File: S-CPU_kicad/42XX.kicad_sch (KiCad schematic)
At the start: 161 parts, among them U34 OR_2, U35 OR_2, U36 OR_2, U37 OR_2, U6 MUX, U6 MUXI

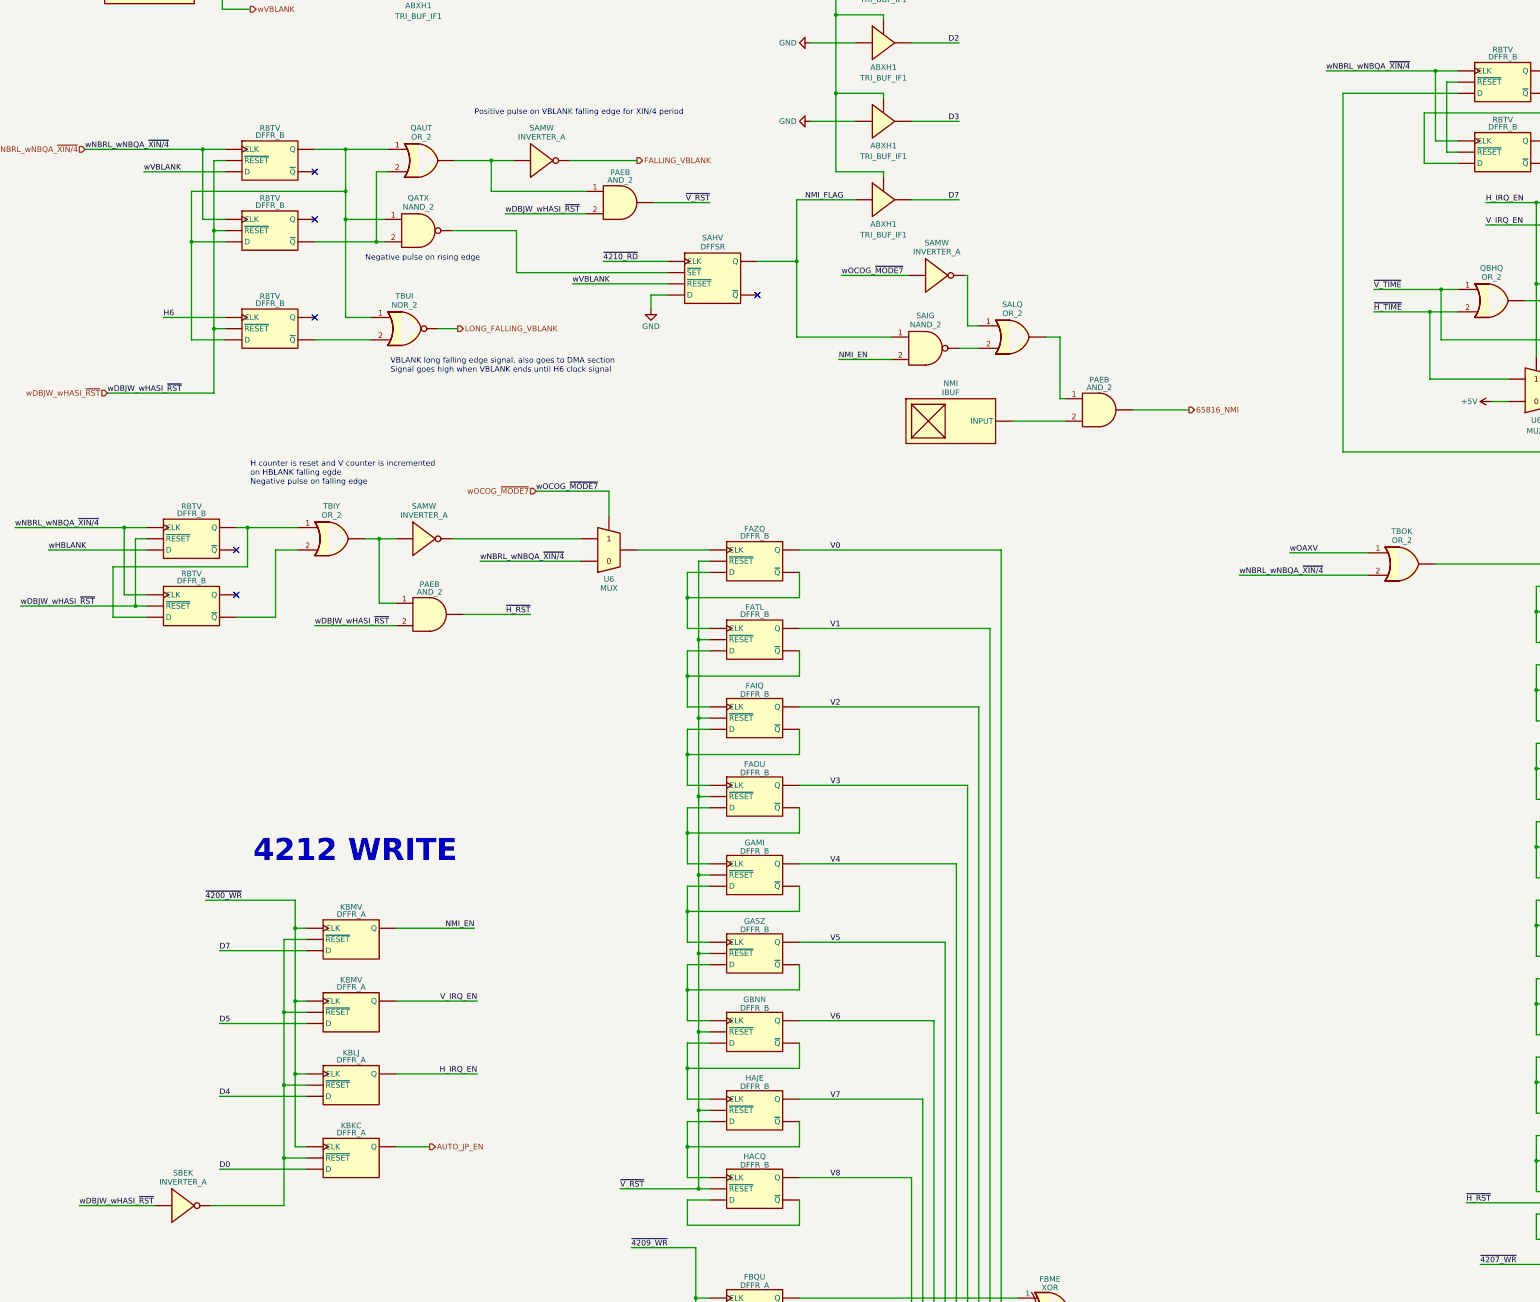
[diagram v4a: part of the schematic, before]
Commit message: Identified some DFFs as being DFFs with SET input rather than RESET input. It helps explaining a lot of beahiour in the MUL/DIV section and in the DMA section.
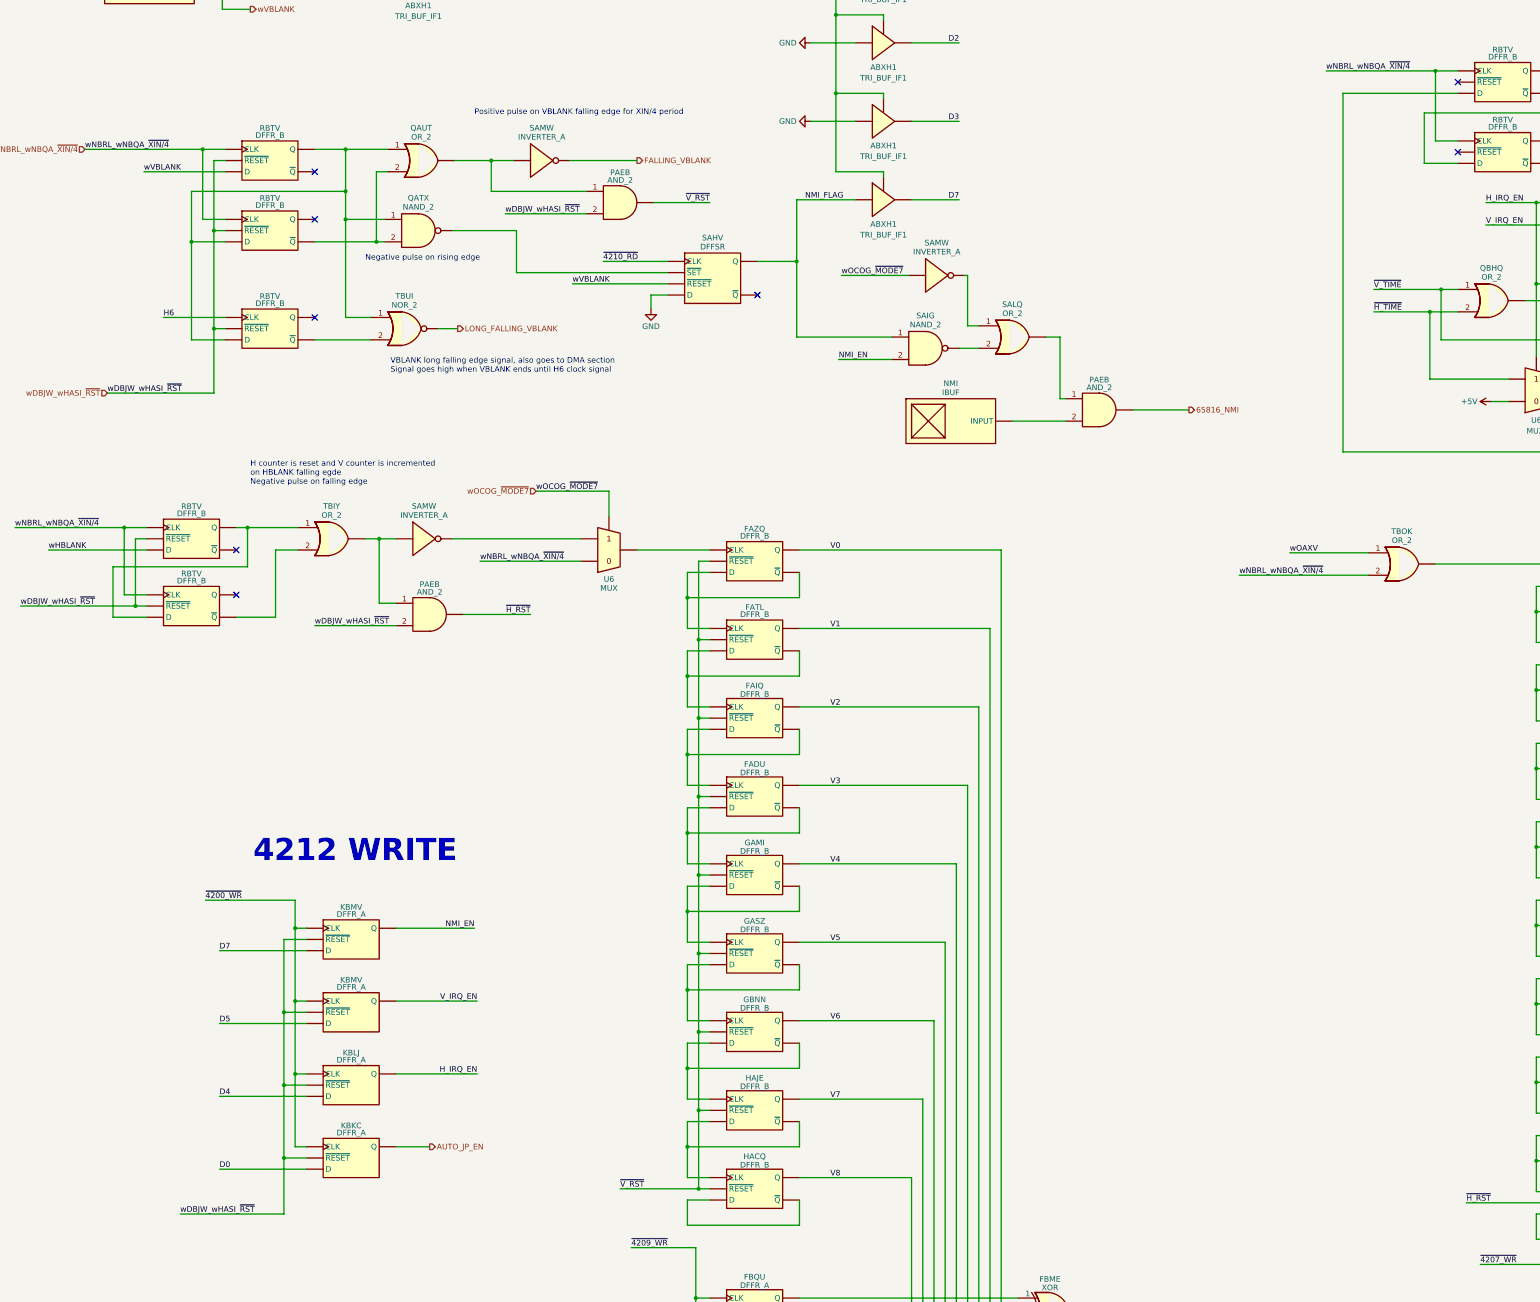
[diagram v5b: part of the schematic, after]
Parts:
- removed SBEK: INVERTER_A, symbol Ricoh_Cells:INVERTER_A
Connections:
- net wDBJW_wHASI_~{RST}: now also KBKC.1 (~{RESET}), KBKC.5 (~{RESET}), KBLJ.1 (~{RESET}), KBLJ.5 (~{RESET}), KBMV.1 (~{RESET}), KBMV.1 (~{RESET}), KBMV.5 (~{RESET}), KBMV.5 (~{RESET})
- net at RBTV.1 (~{RESET}), RBTV.5 (~{RESET}): no longer RBTV.1 (~{RESET}), RBTV.5 (~{RESET})
- new net: RBTV.1 (~{RESET}), RBTV.5 (~{RESET})
- no-connect marks 26 -> 28
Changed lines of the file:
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@@
   (no_connect (at 415.29 476.25))
   (no_connect (at 607.695 400.05))
+  (no_connect (at 584.835 133.985))
   (no_connect (at 325.755 149.225))
   (no_connect (at 415.29 503.555))
@@
   (no_connect (at 415.29 422.91))
   (no_connect (at 325.755 171.45))
+  (no_connect (at 584.835 118.11))
   (no_connect (at 607.695 507.365))
   (no_connect (at 415.29 396.24))
@@
     (stroke (width 0) (type default))
   )
-  (wire (pts (xy 302.26 372.745) (xy 318.77 372.745))
-    (stroke (width 0) (type default))
-  )
   (wire (pts (xy 406.4 412.115) (xy 415.29 412.115))
     (stroke (width 0) (type default))
@@
     (stroke (width 0) (type default))
   )
-  (wire (pts (xy 584.835 133.985) (xy 582.295 133.985))
-    (stroke (width 0) (type default))
-  )
   (wire (pts (xy 120.015 500.38) (xy 147.32 500.38))
     (stroke (width 0) (type default))
@@
     (stroke (width 0) (type default))
   )
-  (wire (pts (xy 318.77 361.95) (xy 318.77 372.745))
+  (wire (pts (xy 318.77 361.95) (xy 318.77 374.65))
     (stroke (width 0) (type default))
   )
@@
     (stroke (width 0) (type default))
   )
-  (wire (pts (xy 582.295 133.985) (xy 582.295 118.11))
-    (stroke (width 0) (type default))
-  )
   (wire (pts (xy 304.8 77.47) (xy 304.8 83.82))
     (stroke (width 0) (type default))
@@
     (stroke (width 0) (type default))
   )
-  (wire (pts (xy 272.415 372.745) (xy 289.56 372.745))
+  (wire (pts (xy 295.275 374.65) (xy 318.77 374.65))
     (stroke (width 0) (type default))
   )
@@
     (stroke (width 0) (type default))
   )
-  (wire (pts (xy 584.835 118.11) (xy 582.295 118.11))
-    (stroke (width 0) (type default))
-  )
   (wire (pts (xy 481.33 224.155) (xy 435.61 224.155))
     (stroke (width 0) (type default))
@@
     (effects (font (size 1.27 1.27)) (justify right bottom))
   )
-  (label "wDBJW_wHASI_~{RST}" (at 272.415 372.745 0) (fields_autoplaced)
+  (label "wDBJW_wHASI_~{RST}" (at 295.275 374.65 0) (fields_autoplaced)
     (effects (font (size 1.27 1.27)) (justify left bottom))
   )
@@
         )
       )
-    )
-  )
-  (symbol (lib_id "Ricoh_Cells:INVERTER_A") (at 295.91 372.745 0) (unit 1)
-    (in_bom yes) (on_board yes) (dnp no) (fields_autoplaced)
-    (property "Reference" "SBEK" (at 295.91 365.355 0)
-      (effects (font (size 1.27 1.27)))
-    )
-    (property "Value" "INVERTER_A" (at 295.91 367.403 0)
-      (effects (font (size 1.27 1.27)))
-    )
-    (property "Footprint" "" (at 293.37 372.745 0)
-      (effects (font (size 1.27 1.27)) hide)
-    )
-    (property "Datasheet" "http://iceboy.a-singer.de/doc/dmg_cells.html#inv_a" (at 297.18 380.365 0)
-      (effects (font (size 1.27 1.27)) hide)
-    )
-    (pin "1")
-    (pin "2")
-    (instances
-      (project "S-CPU"
-        (path "/ca9d3ca9-0297-4b98-a109-b7c162ccc5c3/c42cdb83-bc69-486b-820b-017180bd7612"
-          (reference "SBEK") (unit 1)
-        )
-        (path "/ca9d3ca9-0297-4b98-a109-b7c162ccc5c3/4dc5cd9a-499d-4e55-930f-d6021c4e63f2"
-          (reference "SBEK") (unit 1)
-        )
-      )

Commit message: Fix ERC errors in schematics.
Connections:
- net wOAXV: now also U6.1
- net wOCOG_~{MODE7}: no longer U6.1
- net 65816_IRQ renamed 65816_~{IRQ}
- net 65816_NMI renamed 65816_~{NMI}
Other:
- title: SNES S-CPU Schematics  -> Reverse Engineered SNES S-CPU Schematics 
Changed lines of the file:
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@@
   (paper "A1")
   (title_block
-    (title "SNES S-CPU Schematics ")
+    (title "Reverse Engineered SNES S-CPU Schematics ")
     (date "2023-10-21")
     (rev "0.1")
@@
     (stroke (width 0) (type default))
   )
-  (wire (pts (xy 445.135 161.925) (xy 460.375 161.925))
+  (wire (pts (xy 445.77 161.925) (xy 460.375 161.925))
     (stroke (width 0) (type default))
   )
@@
     (effects (font (size 1.27 1.27)) (justify left bottom))
   )
-  (label "wOAXV" (at 546.735 224.79 0) (fields_autoplaced)
-    (effects (font (size 1.27 1.27)) (justify left bottom))
-  )
   (label "H6" (at 291.465 171.45 0) (fields_autoplaced)
     (effects (font (size 1.27 1.27)) (justify left bottom))
@@
     (effects (font (size 1.27 1.27)) (justify left bottom))
   )
-  (label "wOCOG_~{MODE7}" (at 445.135 161.925 0) (fields_autoplaced)
+  (label "wOCOG_~{MODE7}" (at 445.77 161.925 0) (fields_autoplaced)
     (effects (font (size 1.27 1.27)) (justify left bottom))
   )
@@
     (effects (font (size 1.27 1.27)) (justify right bottom))
   )
-  (label "wOCOG_~{MODE7}" (at 375.92 210.82 0) (fields_autoplaced)
-    (effects (font (size 1.27 1.27)) (justify left bottom))
-  )
   (label "~{4208_WR}" (at 593.09 504.825 0) (fields_autoplaced)
     (effects (font (size 1.27 1.27)) (justify left bottom))
@@
     (effects (font (size 1.27 1.27)) (justify right bottom))
   )
-  (hierarchical_label "65816_NMI" (shape output) (at 523.875 192.405 0) (fields_autoplaced)
+  (hierarchical_label "65816_~{NMI}" (shape output) (at 523.875 192.405 0) (fields_autoplaced)
     (effects (font (size 1.27 1.27)) (justify left))
   )
@@
     (effects (font (size 1.27 1.27)) (justify left))
   )
-  (hierarchical_label "wOCOG_~{MODE7}" (shape input) (at 375.92 210.82 180) (fields_autoplaced)
-    (effects (font (size 1.27 1.27)) (justify right))
-  )
   (hierarchical_label "AUTO_JP_READING" (shape input) (at 311.15 59.69 180) (fields_autoplaced)
     (effects (font (size 1.27 1.27)) (justify right))
@@
     (effects (font (size 1.27 1.27)) (justify right))
   )
+  (hierarchical_label "wOAXV" (shape input) (at 546.735 224.79 180) (fields_autoplaced)
+    (effects (font (size 1.27 1.27)) (justify right))
+  )
   (hierarchical_label "LONG_FALLING_VBLANK" (shape output) (at 358.14 173.99 0) (fields_autoplaced)
     (effects (font (size 1.27 1.27)) (justify left))
@@
     (effects (font (size 1.27 1.27)) (justify right))
   )
+  (hierarchical_label "wOCOG_~{MODE7}" (shape input) (at 445.77 161.925 180) (fields_autoplaced)
+    (effects (font (size 1.27 1.27)) (justify right))
+  )
   (hierarchical_label "wHBLANK" (shape output) (at 311.15 83.82 0) (fields_autoplaced)
     (effects (font (size 1.27 1.27)) (justify left))
@@
     (effects (font (size 1.27 1.27)) (justify left))
   )
-  (hierarchical_label "65816_IRQ" (shape output) (at 755.015 181.61 0) (fields_autoplaced)
+  (hierarchical_label "65816_~{IRQ}" (shape output) (at 755.015 181.61 0) (fields_autoplaced)
     (effects (font (size 1.27 1.27)) (justify left))
   )
+  (hierarchical_label "wOAXV" (shape input) (at 375.92 210.82 180) (fields_autoplaced)
+    (effects (font (size 1.27 1.27)) (justify right))
+  )
   (symbol (lib_id "Ricoh_Cells:DFFR_B") (at 425.45 315.595 0) (unit 1)

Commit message: Big rework on the hierachical sheet to make thigs a bit clearer. PDF exported for Rev 0.1.
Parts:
- renumbered DCFC to DADP, JP2I0 to HBLANK, U37 to HFCV, U35 to HFDV, U36 to HFET, U34 to HFOS, U36 to HHKW, U34 to HHOJ, HFWL to MFAE, HFWL to NFBB, SAMW to PBHU, SAMW to QAAG, SAMW to QANN, SAMW to QAZI, PAEB to QBBI, SAMW to QBDD, SAMW to QBKI, KBMV to SAND, KBLJ to SAUU, KBKC to SAWH, KBMV to SAWV, U6 to SBFO0, U6 to SBFO1, U6 to SBFU, RBTV to SBMW, RBTV to SBPL, ABXH1 to TAAD0, ABXH1 to TAAD1, ABWF1 to TAAD2, ABVA1 to TAAD3, ABXH1 to TAAD4, RBTV to TAOI, RBTV to TAQM, ABXH1 to TAXO0, ABWF1 to TAXO1, ABVA1 to TAXO2, RBTV to TBHT, RBTV to TBIG, SAMW to TBML, PAEB to TBOC, U6 to TBPX, RBTV to TBTP, ABVA1 to TBVD, JP2I0 to VBLANK
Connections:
- net AUTO_JP_EN: now also SAWH.9 (Q); no longer SAWH.6 (Q)
- net H0: now also RBTV.9 (Q); no longer RBTV.7 (Q)
- net H1: now also RBSA.9 (Q); no longer RBSA.7 (Q)
- net H2: now also RBPF.9 (Q); no longer RBPF.7 (Q)
- net H3: now also RBFP.9 (Q); no longer RBFP.7 (Q)
- net H4: now also RBAH.9 (Q); no longer RBAH.7 (Q)
- net H5: now also RAUW.9 (Q); no longer RAUW.7 (Q)
- net H6: now also RARK.9 (Q), TBTP.1 (CLK); no longer RARK.7 (Q), TBTP.3 (CLK), TBTP.4 (~{CLK})
- net H7: now also RAIH.9 (Q); no longer RAIH.7 (Q)
- net H8: now also RACU.9 (Q); no longer RACU.7 (Q)
- net H_IRQ_EN: now also SAUU.9 (Q); no longer SAUU.6 (Q)
- net IRQ_FLAG: now also SBRW.11 (Q); no longer SBRW.5 (Q)
- net NMI_EN: now also SAND.9 (Q); no longer SAND.6 (Q)
- net NMI_FLAG: now also SAHV.11 (Q); no longer SAHV.5 (Q)
- net V0: now also FAZQ.9 (Q); no longer FAZQ.7 (Q)
- net V1: now also FATL.9 (Q); no longer FATL.7 (Q)
- net V2: now also FAIQ.9 (Q); no longer FAIQ.7 (Q)
- net V3: now also FADU.9 (Q); no longer FADU.7 (Q)
- net V4: now also GAMI.9 (Q); no longer GAMI.7 (Q)
- net V5: now also GASZ.9 (Q); no longer GASZ.7 (Q)
- net V6: now also GBNN.9 (Q); no longer GBNN.7 (Q)
- net V7: now also HAJE.9 (Q); no longer HAJE.7 (Q)
- net V8: now also HACQ.9 (Q); no longer HACQ.7 (Q)
- net V_IRQ_EN: now also SAWV.9 (Q); no longer SAWV.6 (Q)
- net wVBLANK: now also SAHV.7 (~{RESET}); no longer SAHV.6 (~{RESET})
- net ~{4200_WR}: now also SAND.1 (CLK), SAUU.1 (CLK), SAWH.1 (CLK), SAWV.1 (CLK); no longer SAND.3 (CLK), SAND.4 (~{CLK}), SAUU.3 (CLK), SAUU.4 (~{CLK}), SAWH.3 (CLK), SAWH.4 (~{CLK}), SAWV.3 (CLK), SAWV.4 (~{CLK})
- net ~{4207_WR}: now also PAEL.1 (CLK), PAGQ.1 (CLK), PAJI.1 (CLK), PAJU.1 (CLK), PBBT.1 (CLK), PBKA.1 (CLK), PBMC.1 (CLK), PBML.1 (CLK); no longer PAEL.3 (CLK), PAEL.4 (~{CLK}), PAGQ.3 (CLK), PAGQ.4 (~{CLK}), PAJI.3 (CLK), PAJI.4 (~{CLK}), PAJU.3 (CLK), PAJU.4 (~{CLK}), PBBT.3 (CLK), PBBT.4 (~{CLK}), PBKA.3 (CLK), PBKA.4 (~{CLK}), PBMC.3 (CLK), PBMC.4 (~{CLK}), PBML.3 (CLK), PBML.4 (~{CLK})
- net ~{4208_WR}: now also PABT.1 (CLK); no longer PABT.3 (CLK), PABT.4 (~{CLK})
- net ~{4209_WR}: now also FBPK.1 (CLK), FBQN.1 (CLK), FBQO.1 (CLK), FBQU.1 (CLK), GBGR.1 (CLK), GBKP.1 (CLK), GBPD.1 (CLK), GBQZ.1 (CLK); no longer FBPK.3 (CLK), FBPK.4 (~{CLK}), FBQN.3 (CLK), FBQN.4 (~{CLK}), FBQO.3 (CLK), FBQO.4 (~{CLK}), FBQU.3 (CLK), FBQU.4 (~{CLK}), GBGR.3 (CLK), GBGR.4 (~{CLK}), GBKP.3 (CLK), GBKP.4 (~{CLK}), GBPD.3 (CLK), GBPD.4 (~{CLK}), GBQZ.3 (CLK), GBQZ.4 (~{CLK})
- net ~{420A_WR}: now also JAKI.1 (CLK); no longer JAKI.3 (CLK), JAKI.4 (~{CLK})
- net ~{4210_RD}: now also SAHV.1 (CLK); no longer SAHV.7 (CLK)
- net ~{4211_RD}: now also SBRW.1 (CLK); no longer SBRW.7 (CLK)
- net ~{H_RST}: now also RACU.6 (~{RESET}), RAIH.6 (~{RESET}), RARK.6 (~{RESET}), RAUW.6 (~{RESET}), RBAH.6 (~{RESET}), RBFP.6 (~{RESET}), RBPF.6 (~{RESET}), RBSA.6 (~{RESET}), RBTV.6 (~{RESET}); no longer RACU.1 (~{RESET}), RACU.5 (~{RESET}), RAIH.1 (~{RESET}), RAIH.5 (~{RESET}), RARK.1 (~{RESET}), RARK.5 (~{RESET}), RAUW.1 (~{RESET}), RAUW.5 (~{RESET}), RBAH.1 (~{RESET}), RBAH.5 (~{RESET}), RBFP.1 (~{RESET}), RBFP.5 (~{RESET}), RBPF.1 (~{RESET}), RBPF.5 (~{RESET}), RBSA.1 (~{RESET}), RBSA.5 (~{RESET}), RBTV.1 (~{RESET}), RBTV.5 (~{RESET})
- net ~{IRQ_FLAG}: now also SBRW.9 (~{Q}); no longer SBRW.4 (~{Q})
- net ~{V_RST}: now also FADU.6 (~{RESET}), FAIQ.6 (~{RESET}), FATL.6 (~{RESET}), FAZQ.6 (~{RESET}), GAMI.6 (~{RESET}), GASZ.6 (~{RESET}), GBNN.6 (~{RESET}), HACQ.6 (~{RESET}), HAJE.6 (~{RESET}); no longer FADU.1 (~{RESET}), FADU.5 (~{RESET}), FAIQ.1 (~{RESET}), FAIQ.5 (~{RESET}), FATL.1 (~{RESET}), FATL.5 (~{RESET}), FAZQ.1 (~{RESET}), FAZQ.5 (~{RESET}), GAMI.1 (~{RESET}), GAMI.5 (~{RESET}), GASZ.1 (~{RESET}), GASZ.5 (~{RESET}), GBNN.1 (~{RESET}), GBNN.5 (~{RESET}), HACQ.1 (~{RESET}), HACQ.5 (~{RESET}), HAJE.1 (~{RESET}), HAJE.5 (~{RESET})
- net at QATX.1, QAUT.1, TAOI.2 (D)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: now also TAQM.9 (Q); no longer TAQM.7 (Q)
- net at QATX.2, QAUT.2: now also TAOI.8 (~{Q}); no longer TAOI.6 (~{Q})
- net at QBJL.2 (1): now also PBKA.9 (Q); no longer PBKA.6 (Q)
- net at PAJU.6 (~{RESET}): no longer QBCM.2 (1)
- net at EAMQ.2 (1): now also FBPK.9 (Q); no longer FBPK.6 (Q)
- net at EALH.2 (1): now also GBPD.9 (Q); no longer GBPD.6 (Q)
- net at JAKI.6 (~{RESET}): no longer GAVG.2 (1)
- net at GBQZ.6 (~{RESET}): no longer DADP.2 (1)
- net at PAEL.6 (~{RESET}): no longer QBJS.2 (1)
- net at QBBT.2 (1): now also PAJI.9 (Q); no longer PAJI.6 (Q)
- net at QBMR.2 (1): now also PAGQ.9 (Q); no longer PAGQ.6 (Q)
- net at PBML.6 (~{RESET}): no longer QBOE.2 (1)
- net at SAHV.4 (~{SET}): now also QATX.3
- net at QBRM.2 (1): now also PBBT.9 (Q); no longer PBBT.6 (Q)
- net at TBML.2: now also TBPX.3; no longer TBPX.2
- net at FBQO.6 (~{RESET}): no longer FBNP.2 (1)
- net ~{MRST}: now reaches TAQM.6 (~{RESET})
- net ~{MRST}: now also QBBI.2, SAND.6 (~{RESET}), SAUU.6 (~{RESET}), SAWH.6 (~{RESET}), SAWV.6 (~{RESET}), TAOI.6 (~{RESET}), TBHT.6 (~{RESET}), TBIG.6 (~{RESET}), TBOC.2, TBTP.6 (~{RESET})
- net at TBUI.2: now also TBTP.8 (~{Q}); no longer TBTP.6 (~{Q})
- net at TBIG.2 (D), TBIY.1: now also TBHT.9 (Q); no longer TBHT.7 (Q)
- net at TBIY.2: now also TBIG.8 (~{Q}); no longer TBIG.6 (~{Q})
- net at SBHV.3: now also SBRW.7 (~{RESET}); no longer SBRW.6 (~{RESET})
- net ~{XIN/4}: now reaches SBMW.1 (CLK)
- net ~{XIN/4}: now also SBPL.1 (CLK), TAOI.1 (CLK), TAQM.1 (CLK), TBHT.1 (CLK), TBIG.1 (CLK), TBOK.2, TBPX.2; no longer SBMW.5 (~{RESET})
- net at SBPL.2 (D), SBQS.1: now also SBMW.9 (Q); no longer SBMW.7 (Q)
- net at FBME.2 (1): now also FBQU.9 (Q); no longer FBQU.6 (Q)
- net at HACQ.2 (D): now also HACQ.8 (~{Q}); no longer HACQ.6 (~{Q})
- net at FBQN.6 (~{RESET}): no longer FAMM.2 (1)
- net at QBKC.2 (1): now also PBMC.9 (Q); no longer PBMC.6 (Q)
- net at GBKP.6 (~{RESET}): no longer GBDX.2 (1)
- net at QABF.2 (1): now also PABT.9 (Q); no longer PABT.6 (Q)
- net at SBPL.6 (~{RESET}): no longer SBQS.2
- net at RACU.2 (D): now also RACU.8 (~{Q}); no longer RACU.6 (~{Q})
- net at GBGR.6 (~{RESET}): no longer GAXC.2 (1)
- removed net wDBJW_wHASI_~{RST}: QBBI.2, SAND.1 (~{RESET}), SAND.5 (~{RESET}), SAUU.1 (~{RESET}), SAUU.5 (~{RESET}), SAWH.1 (~{RESET}), SAWH.5 (~{RESET}), SAWV.1 (~{RESET}), SAWV.5 (~{RESET}), TAOI.1 (~{RESET}), TAOI.5 (~{RESET}), TAQM.1 (~{RESET}), TAQM.5 (~{RESET}), TBHT.1 (~{RESET}), TBHT.5 (~{RESET}), TBIG.1 (~{RESET}), TBIG.5 (~{RESET}), TBOC.2, TBTP.1 (~{RESET}), TBTP.5 (~{RESET})
- removed net wNBRL_wNBQA_~{XIN/4}: SBMW.3 (CLK), SBMW.4 (~{CLK}), SBPL.3 (CLK), SBPL.4 (~{CLK}), TAOI.3 (CLK), TAOI.4 (~{CLK}), TAQM.3 (CLK), TAQM.4 (~{CLK}), TBHT.3 (CLK), TBHT.4 (~{CLK}), TBIG.3 (CLK), TBIG.4 (~{CLK}), TBOK.2, TBPX.3
- net wOAXV renamed COUNTER_TEST_MODE
- net wOCOG_~{MODE7} renamed ~{MODE7}
- new net: GAMI.2 (D), GAMI.8 (~{Q}), GASZ.1 (CLK)
- new net: GASZ.2 (D), GASZ.8 (~{Q}), GBNN.1 (CLK)
- new net: FADU.2 (D), FADU.8 (~{Q}), GAMI.1 (CLK)
- new net: PAJU.9 (Q), QBCM.2 (1)
- new net: RARK.1 (CLK), RAUW.2 (D), RAUW.8 (~{Q})
- new net: RAIH.1 (CLK), RARK.2 (D), RARK.8 (~{Q})
- new net: GAVG.2 (1), JAKI.9 (Q)
- new net: DADP.2 (1), GBQZ.9 (Q)
- new net: FAZQ.1 (CLK), TBPX.4
- new net: FATL.1 (CLK), FAZQ.2 (D), FAZQ.8 (~{Q})
- new net: PAEL.9 (Q), QBJS.2 (1)
- new net: RBTV.1 (CLK), TBOK.3
- new net: PBML.9 (Q), QBOE.2 (1)
- new net: FBNP.2 (1), FBQO.9 (Q)
- new net: RBPF.1 (CLK), RBSA.2 (D), RBSA.8 (~{Q})
- new net: RBFP.1 (CLK), RBPF.2 (D), RBPF.8 (~{Q})
- new net: GBNN.2 (D), GBNN.8 (~{Q}), HAJE.1 (CLK)
- new net: HACQ.1 (CLK), HAJE.2 (D), HAJE.8 (~{Q})
- new net: RBAH.1 (CLK), RBFP.2 (D), RBFP.8 (~{Q})
- new net: FADU.1 (CLK), FAIQ.2 (D), FAIQ.8 (~{Q})
- new net: SBQS.3, SBRW.4 (~{SET})
- new net: FAIQ.1 (CLK), FATL.2 (D), FATL.8 (~{Q})
- new net: RACU.1 (CLK), RAIH.2 (D), RAIH.8 (~{Q})
- new net: FAMM.2 (1), FBQN.9 (Q)
- new net: RBSA.1 (CLK), RBTV.2 (D), RBTV.8 (~{Q})
- new net: RAUW.1 (CLK), RBAH.2 (D), RBAH.8 (~{Q})
- new net: GBDX.2 (1), GBKP.9 (Q)
- new net: SBPL.8 (~{Q}), SBQS.2
- new net: GAXC.2 (1), GBGR.9 (Q)
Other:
- added sheet DIVISION QUOTIENT REGISTERS (divquotient.kicad_sch)
- added sheet MUL PRODUCT OR DIV REMAINDER REGISTERS (productremainder.kicad_sch)
- note added: "MULTIPLICATION & DIVISION"
- moved on the sheet: HFCV, HFDV, HFET, HFOS, HFWL, HHKW, HHOJ, IRQ, MFAE, NFBB, QAGL, QAJG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

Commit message: Fixed VAWR which should have been an SR DFF (to fix issue #3 raised in github)
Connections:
- net A0: now also UBET.1 (IN1); no longer UBET. (~{OUT1})
- net A1: now also UBEF.1 (IN1); no longer UBEF. (~{OUT1})
- net A2: now also UBDP.1 (IN1); no longer UBDP. (~{OUT1})
- net at UAAQ.4, UAWA.2, UBAQ.2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: now also UBDP.3 (~{OUT1}); no longer UBDP. (~{OUT1})
- net at UAAQ.3, UAND.3, UAPQ.3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: now also UBEF.3 (~{OUT1}); no longer UBEF. (~{OUT1})
- net at UAAQ.2, UAFT.2, UAPD.2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: now also UBET.3 (~{OUT1}); no longer UBET. (~{OUT1})
- net at UAAW.1, UAFT.1, UAND.1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: now also UBDP.2 (~{OUT0}); no longer UBDP. (~{OUT1})
- net at UAAW.2, UAND.2, UANF.2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: now also UBET.2 (~{OUT0}); no longer UBET. (~{OUT1})
- net at UAAW.3, UAFT.3, UANF.3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: now also UBEF.2 (~{OUT0}); no longer UBEF. (~{OUT1})
- net at FBME.1: now also FBKE.1; no longer FBKE.2
- net at FBNP.1: now also FBKE.2; no longer FBKE.1
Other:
- moved on the sheet: DADP, EAEJ, EALH, EAMQ, FADU, FAIQ, FALY, FAMM, FAOQ, FATL, FAZQ, FBKE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
